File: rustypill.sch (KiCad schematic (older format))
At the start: 40 parts, among them IC1 DS3231, J1 USB_B_Micro, J2 Conn_01x04, J3 Conn_01x16, J4 Conn_01x16, SW1 Reset, U1 AMS1117-3.3, U2 AT24C512C-SSHD-T, U3 ESP-12F, U4 STM32F103C8Tx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

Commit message: ...
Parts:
- U4: footprint Housings_QFP:LQFP-48_7x7mm_Pitch0.5mm -> STM32F103C8T6:QFP50P900X900X160-48N
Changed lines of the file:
@@
 F 0 "U4" H 8800 1961 50  0000 C CNN
 F 1 "STM32F103C8Tx" H 8800 1870 50  0000 C CNN
-F 2 "Housings_QFP:LQFP-48_7x7mm_Pitch0.5mm" H 8250 2150 50  0001 R CNN
+F 2 "STM32F103C8T6:QFP50P900X900X160-48N" H 8250 2150 50  0001 R CNN
 F 3 "http://www.st.com/st-web-ui/static/active/en/resource/technical/document/datasheet/CD00161566.pdf" H 8850 3550 50  0001 C CNN
 	1    8850 3550

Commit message: ...
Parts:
- added C15: 100nF, Capacitors_SMD:C_0805_HandSoldering, symbol Device:C
- added J5: LCD1602, lib:PinHeader_1x16_P2.54mm_Vertical, symbol Connector_Generic:Conn_01x16
- added J6: IDC_10P, lib:IDC-Header_2x05_P2.54mm_Vertical, symbol Connector_Generic:Conn_02x05_Top_Bottom
- added R13: RCON, Resistors_SMD:R_0805_HandSoldering, symbol Device:R_Small
- added R14: 10k, Resistors_SMD:R_0805_HandSoldering, symbol Device:R_Small
- J1: value USB_B_Micro -> USB
- J2: value Conn_01x04 -> PROG
- J3: value Conn_01x16 -> GPIOB
- J4: value Conn_01x16 -> GPIOA
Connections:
- net +3V3: now also J5.15 (Pin_15), R14.1
- net 32KHZ_IN: no longer J4.9 (Pin_9), U4.29 (PA8)
- net A0: now also J6.1 (Pin_1)
- net A1: now also J6.2 (Pin_2)
- net A15: now also J5.14 (Pin_14)
- net A2: now also J6.3 (Pin_3)
- net A3: now also J6.4 (Pin_4)
- net A4: now also J6.6 (Pin_6)
- net A5: now also J6.7 (Pin_7)
- net A6: now also J6.8 (Pin_8)
- net A7: now also J6.9 (Pin_9)
- net B12: now also J5.4 (Pin_4)
- net B13: now also J5.5 (Pin_5)
- net B14: now also J5.6 (Pin_6)
- net B15: now also J5.16 (Pin_16)
- net B3: now also J5.11 (Pin_11)
- net B4: now also J5.12 (Pin_12)
- net B5: now also J5.13 (Pin_13)
- net GND: now also C15.1, J5.1 (Pin_1), J6.10 (Pin_10), R13.1
- net USB_DP: now also R14.2
- net VPP: now also C15.2, J5.2 (Pin_2), J6.5 (Pin_5)
- new net: J5.3 (Pin_3), R13.2
- new net A8: J4.9 (Pin_9), U4.29 (PA8)
- no-connect marks 19 -> 23
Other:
- moved on the sheet: R10, R11, R12, R7, R9

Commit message: finish v0.1.0
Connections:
- net A8 is gone; now on net 32KHZ_IN: J4.9 (Pin_9), U4.29 (PA8)
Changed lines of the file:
@@
 	0    1    1    0
-$EndComp
-$Comp
-L MCU_ST_STM32F1:STM32F103C8Tx U4
-U 1 1 5DCDB777
-P 8850 3550
-F 0 "U4" H 8800 1961 50  0000 C CNN
-F 1 "STM32F103C8Tx" H 8800 1870 50  0000 C CNN
-F 2 "STM32F103C8T6:QFP50P900X900X160-48N" H 8250 2150 50  0001 R CNN
-F 3 "http://www.st.com/st-web-ui/static/active/en/resource/technical/document/datasheet/CD00161566.pdf" H 8850 3550 50  0001 C CNN
-	1    8850 3550
-	1    0    0    -1
 $EndComp
 Wire Wire Line
@@
 $EndComp
 Wire Wire Line
-	9600 4150 10500 4150
-Wire Wire Line
 	10500 4150 10500 3950
-Connection ~ 10500 4150
 Wire Wire Line
 	10500 4150 10600 4150
@@
 	9450 4450 10150 4450
 Wire Wire Line
-	9450 4550 10150 4550
-Wire Wire Line
 	10350 4450 10600 4450
 Wire Wire Line
@@
 	2750 6450 2800 6450
 Wire Wire Line
-	9450 4150 9500 4150
+	9450 4150 10500 4150
+Connection ~ 10500 4150
+$Comp
+L MCU_ST_STM32F1:STM32F103C8Tx U4
+U 1 1 5DCDB777
+P 8850 3550
+F 0 "U4" H 8800 1961 50  0000 C CNN
+F 1 "STM32F103C8Tx" H 8800 1870 50  0000 C CNN
+F 2 "STM32F103C8T6:QFP50P900X900X160-48N" H 8250 2150 50  0001 R CNN
+F 3 "http://www.st.com/st-web-ui/static/active/en/resource/technical/document/datasheet/CD00161566.pdf" H 8850 3550 50  0001 C CNN
+	1    8850 3550
+	1    0    0    -1
+$EndComp
+Wire Wire Line
+	9450 4550 10150 4550
 $EndSCHEMATC

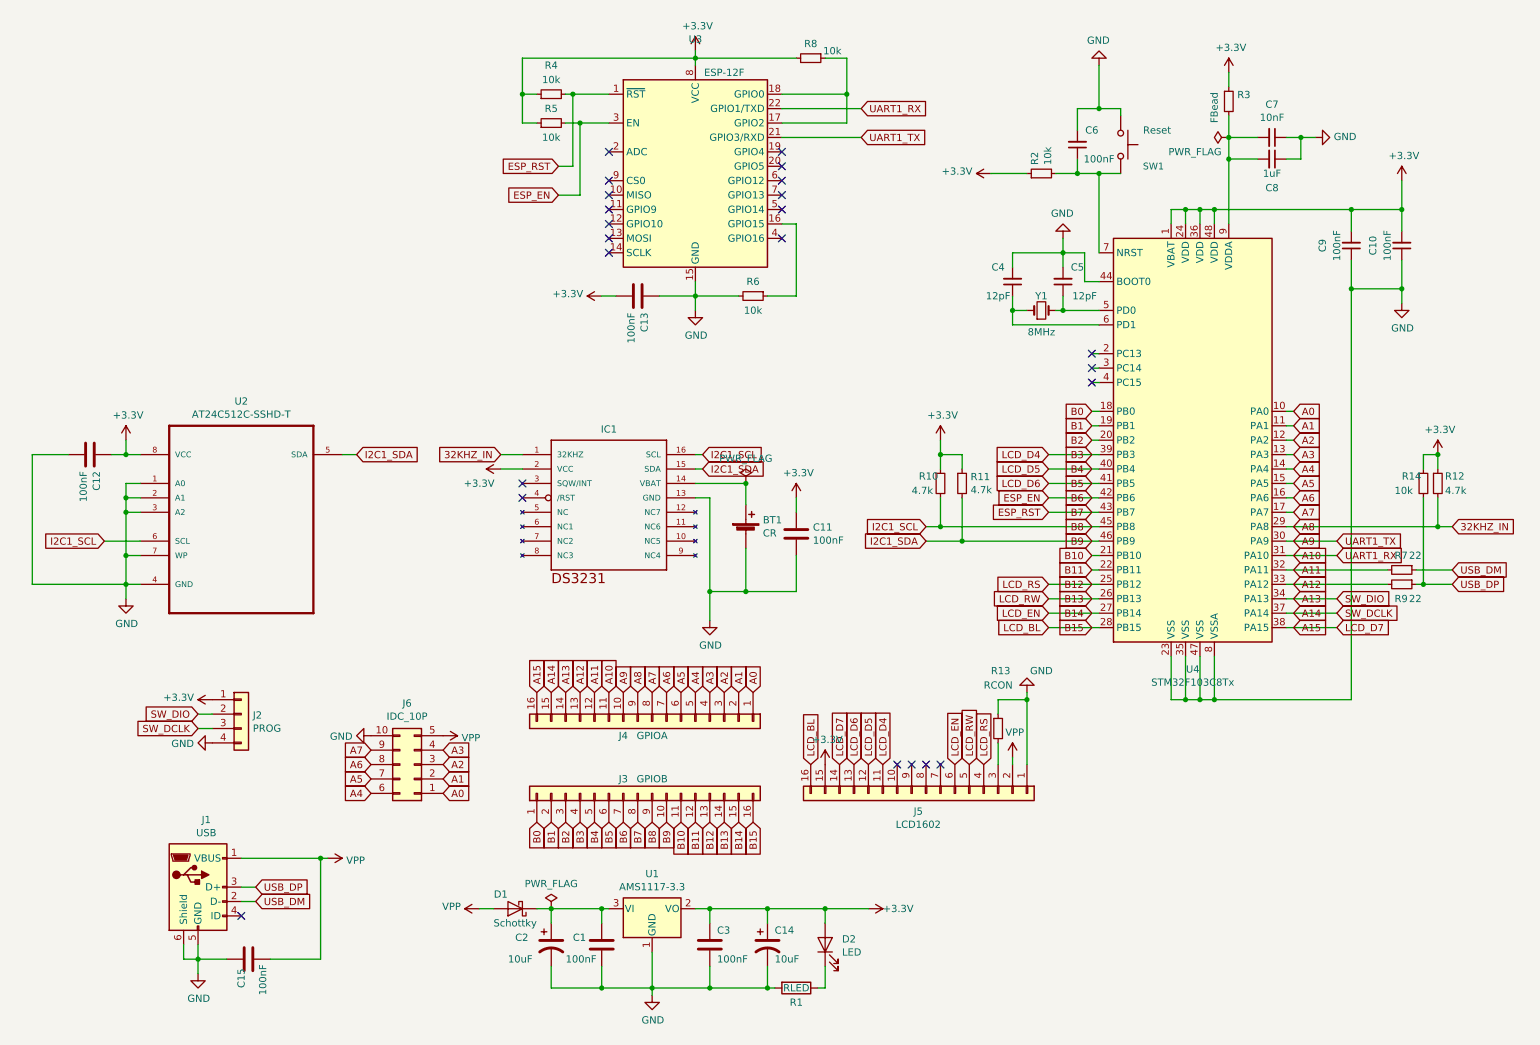
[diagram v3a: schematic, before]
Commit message: add more I2C features; better placement; etc
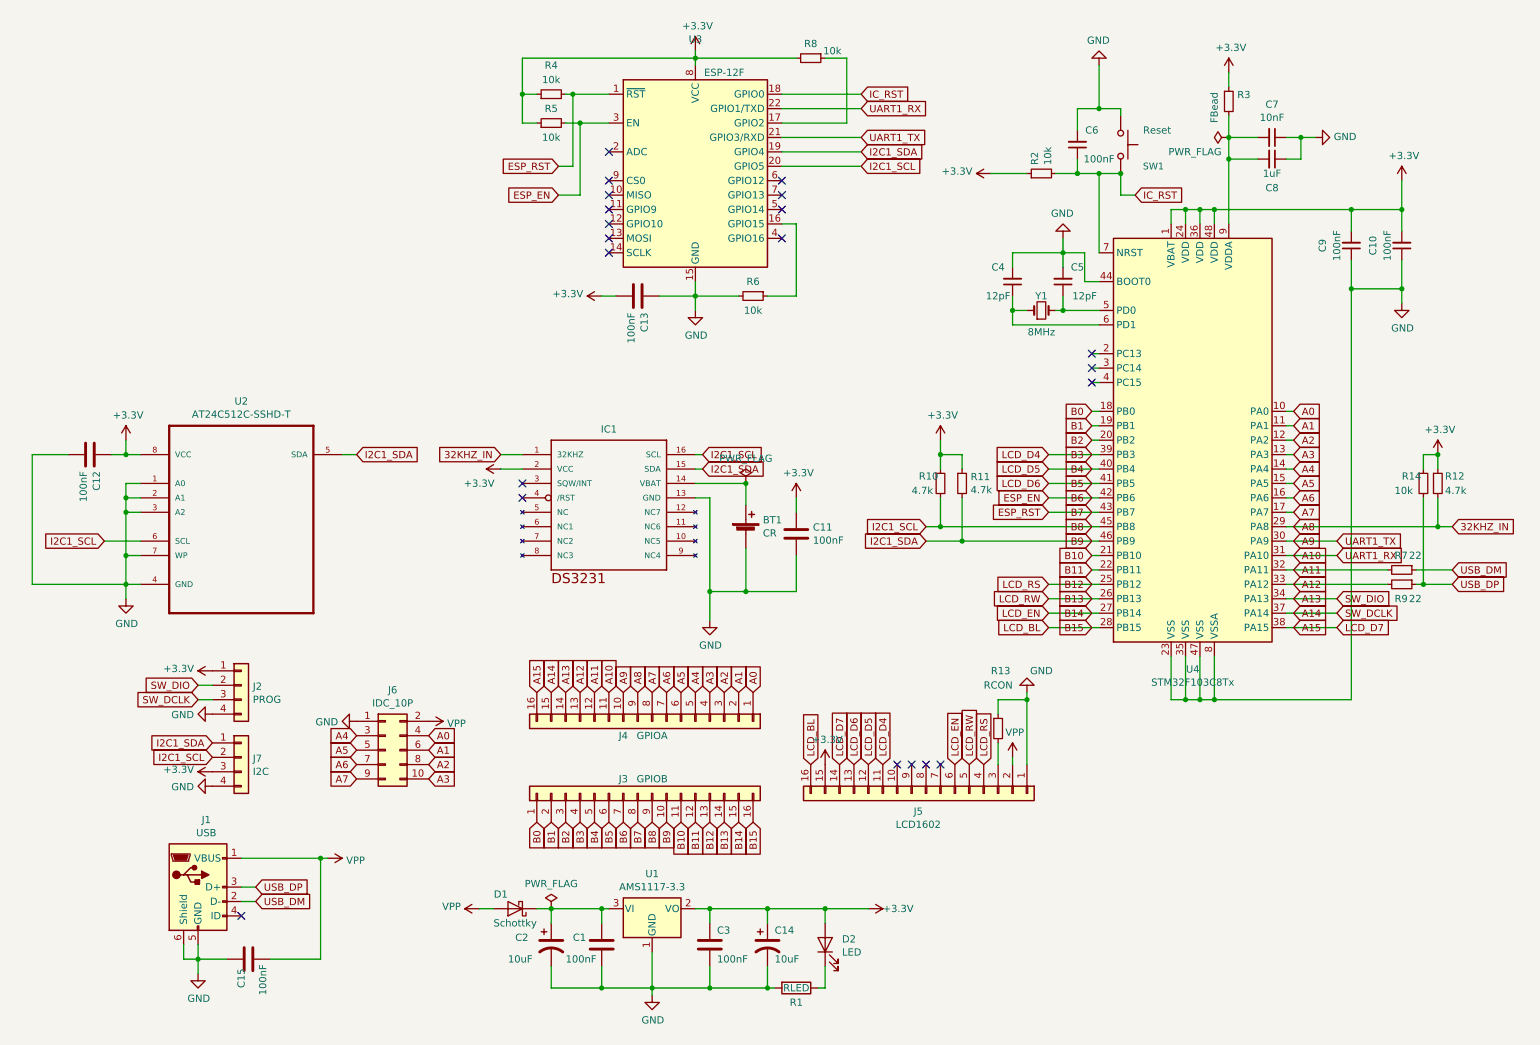
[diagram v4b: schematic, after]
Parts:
- removed J6: IDC_10P, lib:IDC-Header_2x05_P2.54mm_Vertical, symbol Connector_Generic:Conn_02x05_Top_Bottom
- added J6: IDC_10P, lib:IDC-Header_2x05_P2.54mm_Vertical, symbol Connector_Generic:Conn_02x05_Odd_Even
- added J7: I2C, lib:PinHeader_1x04_P2.54mm_Vertical, symbol Connector_Generic:Conn_01x04
- BT1: footprint Connectors:CR2032H -> lib:my3034_holder
- Y1: footprint Oscillators:Oscillator_SMD_Abracon_ASE-4pin_3.2x2.5mm_HandSoldering -> Crystals:Crystal_SMD_5032-2pin_5.0x3.2mm_HandSoldering
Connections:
- net +3V3: now also J7.3 (Pin_3)
- net A0: now also J6.4 (Pin_4)
- net A1: now also J6.6 (Pin_6)
- net A2: now also J6.8 (Pin_8)
- net A3: now also J6.10 (Pin_10)
- net A4: now also J6.3 (Pin_3)
- net A5: now also J6.5 (Pin_5)
- net A6: now also J6.7 (Pin_7)
- net A7: now also J6.9 (Pin_9)
- net B8: now also U3.20 (GPIO5), J7.2 (Pin_2)
- net B9: now also U3.19 (GPIO4), J7.1 (Pin_1)
- net GND: now also J6.1 (Pin_1), J7.4 (Pin_4)
- net VPP: now also J6.2 (Pin_2)
- net at R8.1, U3.17 (GPIO2): no longer U3.18 (GPIO0)
- net IC_RST: now reaches C6.1, R2.2, SW1.2, U4.7 (NRST)
- net IC_RST: now also U3.18 (GPIO0)
- no-connect marks 23 -> 21
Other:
- moved on the sheet: J2
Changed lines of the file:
@@
-$EndComp
-$Comp
-L RF_Module:ESP-12F U3
-U 1 1 5DC17685
-P 5350 1750
-F 0 "U3" H 5350 2731 50  0000 C CNN
-F 1 "ESP-12F" H 5550 2500 50  0000 C CNN
-F 2 "RF_Modules:ESP-12E" H 5350 1750 50  0001 C CNN
-F 3 "http://wiki.ai-thinker.com/_media/esp8266/esp8266_series_modules_user_manual_v1.1.pdf" H 5000 1850 50  0001 C CNN
-	1    5350 1750
-	1    0    0    -1
 $EndComp
 $Comp
@@
 F 0 "BT1" H 5818 4296 50  0000 L CNN
 F 1 "CR" H 5818 4205 50  0000 L CNN
-F 2 "Connectors:CR2032H" V 5700 4260 50  0001 C CNN
+F 2 "lib:my3034_holder" V 5700 4260 50  0001 C CNN
 F 3 "~" V 5700 4260 50  0001 C CNN
 	1    5700 4200
@@
 F 0 "Y1" H 7750 2750 50  0000 C CNN
 F 1 "8MHz" H 7750 2500 50  0000 C CNN
-F 2 "Oscillators:Oscillator_SMD_Abracon_ASE-4pin_3.2x2.5mm_HandSoldering" H 7750 2650 50  0001 C CNN
+F 2 "Crystals:Crystal_SMD_5032-2pin_5.0x3.2mm_HandSoldering" H 7750 2650 50  0001 C CNN
 F 3 "~" H 7750 2650 50  0001 C CNN
 	1    7750 2650
@@
 	4800 2550 4700 2550
 Wire Wire Line
-	6400 900  6400 1150
-Wire Wire Line
 	5350 900  6050 900
 Wire Wire Line
 	6250 900  6400 900
-Wire Wire Line
-	5950 1150 6400 1150
-Connection ~ 6400 1150
-Wire Wire Line
-	6400 1150 6400 1350
 Wire Wire Line
 	5950 1350 6400 1350
@@
 L Connector_Generic:Conn_01x04 J2
 U 1 1 5E6D49A8
-P 2200 5450
-F 0 "J2" H 2280 5442 50  0000 L CNN
-F 1 "PROG" H 2280 5351 50  0000 L CNN
-F 2 "lib:PinHeader_1x04_P2.54mm_Horizontal" H 2200 5450 50  0001 C CNN
-F 3 "~" H 2200 5450 50  0001 C CNN
-	1    2200 5450
+P 2200 5250
+F 0 "J2" H 2280 5242 50  0000 L CNN
+F 1 "PROG" H 2280 5151 50  0000 L CNN
+F 2 "lib:PinHeader_1x04_P2.54mm_Horizontal" H 2200 5250 50  0001 C CNN
+F 3 "~" H 2200 5250 50  0001 C CNN
+	1    2200 5250
 	1    0    0    -1
 $EndComp
@@
 L power:+3.3V #PWR0104
 U 1 1 5E6F9C97
-P 2000 5350
-F 0 "#PWR0104" H 2000 5200 50  0001 C CNN
-F 1 "+3.3V" V 2015 5478 50  0000 L CNN
-F 2 "" H 2000 5350 50  0001 C CNN
-F 3 "" H 2000 5350 50  0001 C CNN
-	1    2000 5350
+P 2000 5150
+F 0 "#PWR0104" H 2000 5000 50  0001 C CNN
+F 1 "+3.3V" V 2015 5278 50  0000 L CNN
+F 2 "" H 2000 5150 50  0001 C CNN
+F 3 "" H 2000 5150 50  0001 C CNN
+	1    2000 5150
 	0    -1   -1   0
 $EndComp
@@
 L power:GND #PWR0105
 U 1 1 5E6FA9FA
-P 2000 5650
-F 0 "#PWR0105" H 2000 5400 50  0001 C CNN
-F 1 "GND" V 2005 5522 50  0000 R CNN
-F 2 "" H 2000 5650 50  0001 C CNN
-F 3 "" H 2000 5650 50  0001 C CNN
-	1    2000 5650
-	0    1    1    0
-$EndComp
-Text GLabel 1900 5450 0    50   Input ~ 0
+P 2000 5450
+F 0 "#PWR0105" H 2000 5200 50  0001 C CNN
+F 1 "GND" V 2005 5322 50  0000 R CNN
+F 2 "" H 2000 5450 50  0001 C CNN
+F 3 "" H 2000 5450 50  0001 C CNN
+	1    2000 5450
+	0    1    1    0
+$EndComp
+Text GLabel 1900 5250 0    50   Input ~ 0
 SW_DIO
 Wire Wire Line
-	1900 5450 2000 5450
-Text GLabel 1900 5550 0    50   Input ~ 0
+	1900 5250 2000 5250
+Text GLabel 1900 5350 0    50   Input ~ 0
 SW_DCLK
 Wire Wire Line
-	1900 5550 2000 5550
+	1900 5350 2000 5350
 Wire Wire Line
 	8100 2950 8150 2950
@@
 NoConn ~ 5950 1850
 NoConn ~ 5950 1750
-NoConn ~ 5950 1650
-NoConn ~ 5950 1550
 $Comp
 L Connector_Generic:Conn_01x16 J3
@@
 Wire Wire Line
 	7800 3650 8150 3650
-$Comp
-L Connector_Generic:Conn_02x05_Top_Bottom J6
-U 1 1 5DF7B1BC
-P 3400 5800
-F 0 "J6" H 3450 5375 50  0000 C CNN
-F 1 "IDC_10P" H 3450 5466 50  0000 C CNN
-F 2 "lib:IDC-Header_2x05_P2.54mm_Vertical" H 3400 5800 50  0001 C CNN
-F 3 "~" H 3400 5800 50  0001 C CNN
-	1    3400 5800
-	-1   0    0    1
-$EndComp
-Text GLabel 3600 6000 2    50   Input ~ 0
+Text GLabel 3500 5600 2    50   Input ~ 0
 A0
-Text GLabel 3600 5900 2    50   Input ~ 0
-A1
-Text GLabel 3600 5800 2    50   Input ~ 0
-A2
-Text GLabel 3600 5700 2    50   Input ~ 0
-A3
-Text GLabel 3100 6000 0    50   Input ~ 0
+Text GLabel 3000 5600 0    50   Input ~ 0
 A4
-Text GLabel 3100 5900 0    50   Input ~ 0
-A5
-Text GLabel 3100 5800 0    50   Input ~ 0
-A6
-Text GLabel 3100 5700 0    50   Input ~ 0
-A7
 $Comp
 L power:VPP #PWR021
 U 1 1 5DF905F6
-P 3600 5600
-F 0 "#PWR021" H 3600 5450 50  0001 C CNN
-F 1 "VPP" V 3615 5728 50  0000 L CNN
-F 2 "" H 3600 5600 50  0001 C CNN
-F 3 "" H 3600 5600 50  0001 C CNN
-	1    3600 5600
+P 3500 5500
+F 0 "#PWR021" H 3500 5350 50  0001 C CNN
+F 1 "VPP" V 3515 5628 50  0000 L CNN
+F 2 "" H 3500 5500 50  0001 C CNN
+F 3 "" H 3500 5500 50  0001 C CNN
+	1    3500 5500
 	0    1    1    0
 $EndComp
@@
 L power:GND #PWR01
 U 1 1 5DF92D64
-P 3100 5600
-F 0 "#PWR01" H 3100 5350 50  0001 C CNN
-F 1 "GND" V 3105 5472 50  0000 R CNN
-F 2 "" H 3100 5600 50  0001 C CNN
-F 3 "" H 3100 5600 50  0001 C CNN
-	1    3100 5600
+P 3000 5500
+F 0 "#PWR01" H 3000 5250 50  0001 C CNN
+F 1 "GND" V 3005 5372 50  0000 R CNN
+F 2 "" H 3000 5500 50  0001 C CNN
+F 3 "" H 3000 5500 50  0001 C CNN
+	1    3000 5500
 	0    1    1    0
 $EndComp
@@
 Wire Wire Line
 	9450 4550 10150 4550
+Text GLabel 6500 1650 2    50   Input ~ 0
+I2C1_SCL
+$Comp
+L RF_Module:ESP-12F U3
+U 1 1 5DC17685
+P 5350 1750
+F 0 "U3" H 5350 2731 50  0000 C CNN
+F 1 "ESP-12F" H 5550 2500 50  0000 C CNN
+F 2 "RF_Modules:ESP-12E" H 5350 1750 50  0001 C CNN
+F 3 "http://wiki.ai-thinker.com/_media/esp8266/esp8266_series_modules_user_manual_v1.1.pdf" H 5000 1850 50  0001 C CNN
+	1    5350 1750
+	1    0    0    -1
+$EndComp
+Wire Wire Line
+	6500 1650 5950 1650
+Text GLabel 6500 1550 2    50   Input ~ 0
+I2C1_SDA
+Wire Wire Line
+	6500 1550 5950 1550
+Text GLabel 8400 1850 2    50   Input ~ 0
+IC_RST
+Wire Wire Line
+	8400 1850 8300 1850
+Wire Wire Line
+	8300 1850 8300 1700
+Connection ~ 8300 1700
+Text GLabel 6500 1150 2    50   Input ~ 0
+IC_RST
+Wire Wire Line
+	6400 900  6400 1350
+Wire Wire Line
+	6500 1150 5950 1150
+$Comp
+L Connector_Generic:Conn_02x05_Odd_Even J6
+U 1 1 5DE1718D
+P 3200 5700
+F 0 "J6" H 3250 6117 50  0000 C CNN
+F 1 "IDC_10P" H 3250 6026 50  0000 C CNN
+F 2 "lib:IDC-Header_2x05_P2.54mm_Vertical" H 3200 5700 50  0001 C CNN
+F 3 "~" H 3200 5700 50  0001 C CNN
+	1    3200 5700
+	1    0    0    -1
+$EndComp
+Text GLabel 3000 5900 0    50   Input ~ 0
+A7
+Text GLabel 3000 5800 0    50   Input ~ 0
+A6
+Text GLabel 3000 5700 0    50   Input ~ 0
+A5
+Text GLabel 3500 5900 2    50   Input ~ 0
+A3
+Text GLabel 3500 5800 2    50   Input ~ 0
+A2
+Text GLabel 3500 5700 2    50   Input ~ 0
+A1
+$Comp
+L Connector_Generic:Conn_01x04 J7
+U 1 1 5DED0768
+P 2200 5750
+F 0 "J7" H 2280 5742 50  0000 L CNN
+F 1 "I2C" H 2280 5651 50  0000 L CNN
+F 2 "lib:PinHeader_1x04_P2.54mm_Vertical" H 2200 5750 50  0001 C CNN
+F 3 "~" H 2200 5750 50  0001 C CNN
+	1    2200 5750
+	1    0    0    -1
+$EndComp
+Text GLabel 2000 5750 0    50   Input ~ 0
+I2C1_SCL
+Text GLabel 2000 5650 0    50   Input ~ 0
+I2C1_SDA
+$Comp
+L power:+3.3V #PWR0109
+U 1 1 5DEFC130
+P 2000 5850
+F 0 "#PWR0109" H 2000 5700 50  0001 C CNN
+F 1 "+3.3V" V 2015 5978 50  0000 L CNN
+F 2 "" H 2000 5850 50  0001 C CNN
+F 3 "" H 2000 5850 50  0001 C CNN
+	1    2000 5850
+	0    -1   -1   0
+$EndComp
+$Comp
+L power:GND #PWR0110
+U 1 1 5DEFDB77
+P 2000 5950
+F 0 "#PWR0110" H 2000 5700 50  0001 C CNN
+F 1 "GND" V 2005 5822 50  0000 R CNN
+F 2 "" H 2000 5950 50  0001 C CNN
+F 3 "" H 2000 5950 50  0001 C CNN
+	1    2000 5950
+	0    1    1    0
+$EndComp
 $EndSCHEMATC
